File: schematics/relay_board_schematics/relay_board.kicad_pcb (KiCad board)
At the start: 2 copper layers, 45 x 75 mm, 46 parts, among them J1 Programming Header, Q1 MMBF170, Q2 MMBF170, U1 SPST_POWER_RELAY, U2 PIC16F1826-ISO, U3 dpdt_relay, U4 INA180A1, U5 CONN_01x05, U6 INA180A1, U7 CONN_01x05

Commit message: first attempt at rerouting
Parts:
- added D4: D, Diode_SMD:D_SMB_Handsoldering, B.Cu at (153.2, 78.2)
- added D5: BLUE 3.2V 10mA, LED_SMD:LED_1206_3216Metric_Pad1.42x1.75mm_HandSolder, F.Cu at (133.2, 133.5)
- added D6: D, Diode_SMD:D_SMB_Handsoldering, B.Cu at (141.1, 81.9)
- added D7: D, Diode_SMD:D_SMB_Handsoldering, B.Cu at (151.9, 83.0)
- C1, C2, C3: footprint Capacitor_SMD:C_0805_2012Metric_Pad1.15x1.40mm_HandSolder -> Capacitor_SMD:C_0805_2012Metric_Pad1.18x1.45mm_HandSolder
- D2: footprint Diode_THT:D_DO-35_SOD27_P7.62mm_Horizontal -> Diode_SMD:D_SMB_Handsoldering
- D3: footprint LED_SMD:LED_1206_3216Metric_Pad1.42x1.75mm_HandSolder -> Diode_SMD:D_SMB_Handsoldering; moved to B.Cu
- F1: footprint rlcs:littlefuse_01000020Z -> custom:littlefuse_01000020Z
- J1: footprint rlcs:PinHeader_5x2.54_SMD_90deg_952-3198-1-ND -> custom:PinHeader_5x2.54_SMD_90deg_952-3198-1-ND
- P1: renamed from GND      PWR
- P2: renamed from PWR      GND
- R1, R10, R11, R12, R13, R2, R3, R4, R5, R6, R7, R8, R9: footprint Resistor_SMD:R_0805_2012Metric_Pad1.15x1.40mm_HandSolder -> Resistor_SMD:R_0805_2012Metric_Pad1.20x1.40mm_HandSolder
- R14, R15: value 0.02 -> 0.01; footprint Resistor_SMD:R_2512_6332Metric_Pad1.52x3.35mm_HandSolder -> Resistor_SMD:R_2512_6332Metric_Pad1.40x3.35mm_HandSolder
- R16: value R -> 180; footprint Resistor_SMD:R_0805_2012Metric_Pad1.15x1.40mm_HandSolder -> Resistor_SMD:R_0805_2012Metric_Pad1.20x1.40mm_HandSolder
- SW1: renamed from 0   SW1   1; footprint rlcs:DIP_SWITCH_4X2 -> custom:DIP_SWITCH_4X2
- TP0: renamed from GND; footprint Socket_Strips:Socket_Strip_Straight_1x01_Pitch2.54mm -> custom:Socket_Strip_Straight_1x01_Pitch2.54mm
- TP1: renamed from 12V; footprint Socket_Strips:Socket_Strip_Straight_1x01_Pitch2.54mm -> custom:Socket_Strip_Straight_1x01_Pitch2.54mm
- TP2: renamed from 5V; footprint Socket_Strips:Socket_Strip_Straight_1x01_Pitch2.54mm -> custom:Socket_Strip_Straight_1x01_Pitch2.54mm
- TP3: renamed from POWER; footprint Socket_Strips:Socket_Strip_Straight_1x01_Pitch2.54mm -> custom:Socket_Strip_Straight_1x01_Pitch2.54mm
- U1: footprint rlcs:Relay_SPST_G5LE-1A -> custom:Relay_SPST_G5LE-1A
- U2: footprint rlcs:PIC16F1826-ISO -> custom:PIC16F1826-ISO
- U3: footprint rlcs:Relay_DPDT_RT424012F -> custom:Relay_DPDT_RT424012F
- moved D3 57.2 mm to (141.9, 77.1)
- moved C3 20.7 mm to (134.7, 97.5)
- moved C1 12.5 mm to (132.9, 111.4), turned to -90 degrees
- moved C2 8.75 mm to (137.4, 97.5), turned to 90 degrees
- moved P2 5.40 mm to (135.2, 128.9), turned to 90 degrees
- moved G*** 4.76 mm to (147.9, 133.2)
- moved R9 4.11 mm to (165.3, 77.2), turned to 180 degrees
- moved R5 3.70 mm to (163.7, 86.8)
- moved D2 3.54 mm to (148.5, 122.2)
- moved R8 3.16 mm to (159.5, 81.1)
- moved R7 2.46 mm to (159.9, 77.2), turned to 0 degrees
- moved TP2 2.31 mm to (132.1, 92.6)
- moved R13 2.27 mm to (159.6, 113.2), turned to 180 degrees
- moved R12 1.86 mm to (136.4, 132.8), turned to 90 degrees
- moved U4 1.84 mm to (134.1, 86.8)
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- renumbered ACT_PWR to P3
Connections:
- D3 pad 1: Net-(D3-Pad1) -> /G1
- D3 pad 2: Net-(D3-Pad2) -> GND
- P2 pad 1: GND -> Net-(F1-Pad1)
- P2 pad 2: Net-(F1-Pad1) -> GND
- R16 pad 1: Net-(D3-Pad1) -> Net-(D5-Pad1)
- U2 pad 11: Net-(D3-Pad2) -> Net-(D5-Pad2)
- U5 pad 1: /SDA -> +12V
- U5 pad 2: /SCL -> +5V
- U5 pad 4: +5V -> /SCL
- U5 pad 5: +12V -> /SDA
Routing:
- net +5V: track 227.5 -> 194.1 mm, vias 5 -> 3
- net Net-(D3-Pad2): track 29.4 -> 0.00 mm, vias 1 -> 0
- net Net-(D5-Pad2): track 0.00 -> 27.6 mm, vias 0 -> 3
- net GND: track 200.4 -> 186.5 mm, vias 8 -> 7
- net Net-(D5-Pad1): track 0.00 -> 8.02 mm
- net Net-(D3-Pad1): track 7.92 -> 0.00 mm
- net Net-(R14-Pad2): track 37.6 -> 29.8 mm
- net Net-(D2-Pad2): track 16.1 -> 23.6 mm
- net /G1: track 31.6 -> 39.0 mm
- net +12V: track 117.7 -> 110.6 mm
- net /G2: track 20.4 -> 26.5 mm
- net /P2: track 19.8 -> 24.5 mm
- net /CURR_SENSE_2: track 23.7 -> 27.9 mm
- net /SELECT: track 43.2 -> 39.1 mm
- net Net-(F1-Pad2): track 29.8 -> 26.4 mm
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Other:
- board text added: "RLCS Relay Board"
- board text removed: "P1"
- board text removed: "RLCS rev3 Hokkaido Aidan Ha 2020-02-02"

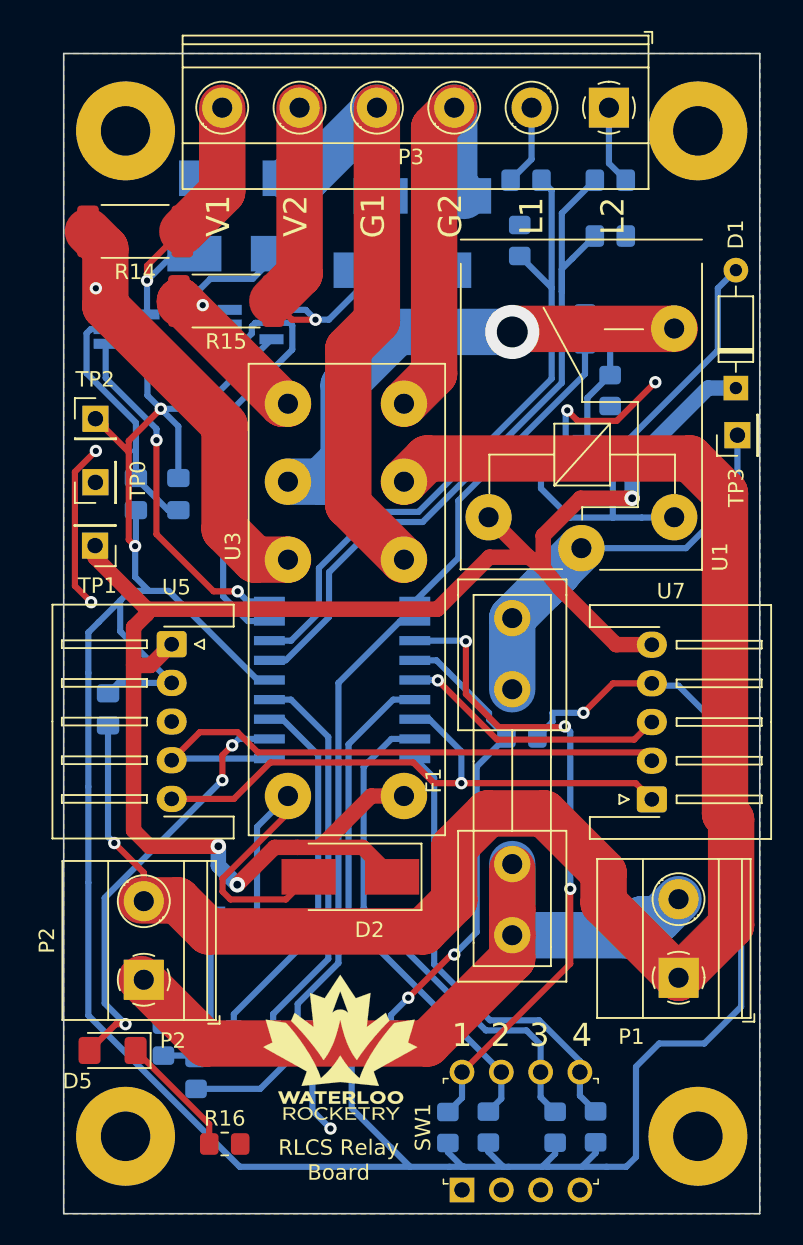
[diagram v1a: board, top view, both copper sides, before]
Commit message: fixed reversed 12V power connectors and cleaned up silkscreens
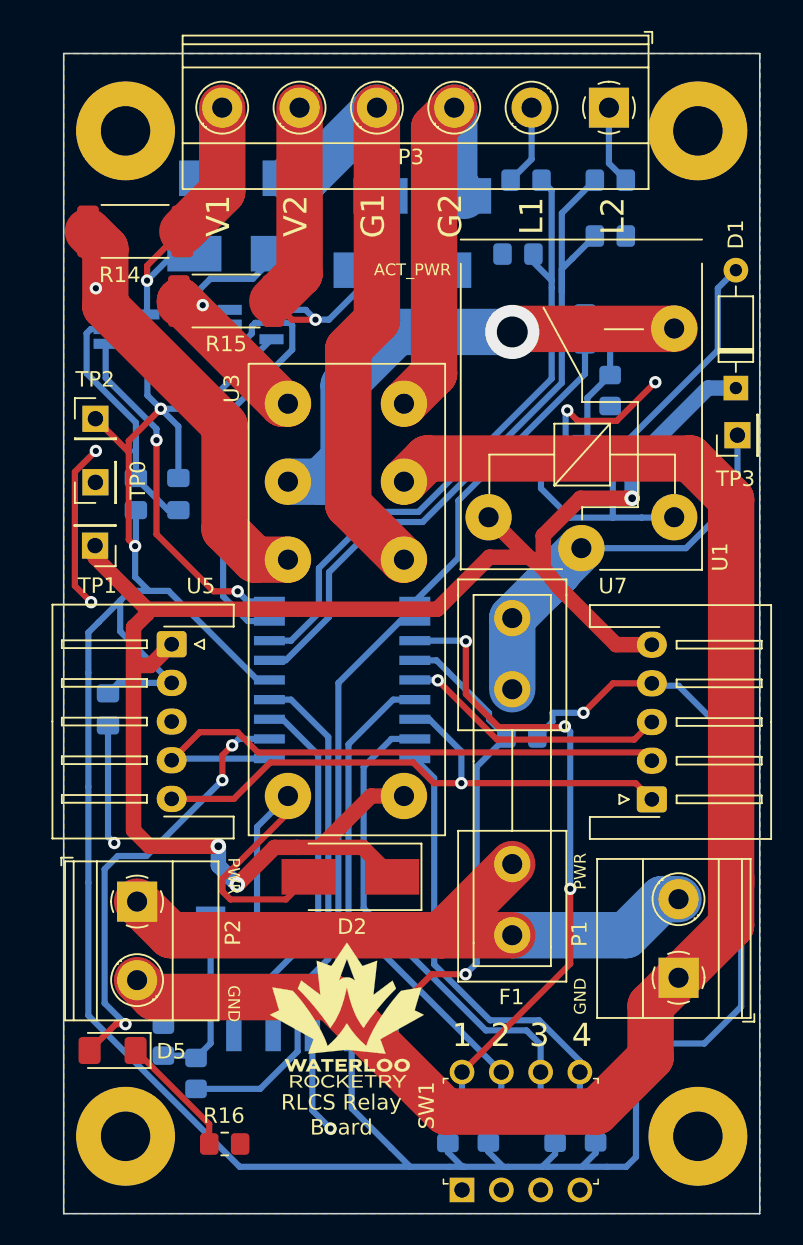
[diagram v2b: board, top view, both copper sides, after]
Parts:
- moved P2 5.07 mm to (134.7, 123.8), turned to -90 degrees
- moved G*** 2.13 mm to (148.3, 131.2)
- moved R8 0.89 mm to (159.4, 82.0), turned to 180 degrees
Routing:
- net Net-(F1-Pad1): track 50.1 -> 43.4 mm
- net GND: track 186.5 -> 180.3 mm
- net /~{MCLR}: track 30.7 -> 31.9 mm
- net Net-(D5-Pad2): track 27.6 -> 28.7 mm
- net +5V: track 194.1 -> 193.4 mm
- net /LIM1: track 43.0 -> 42.3 mm
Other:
- board text added: "ACT_PWR"
- board text added: "GND"
- board text added: "PWR"
- board text removed: "P2"

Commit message: addressed Jack's comments on pcb
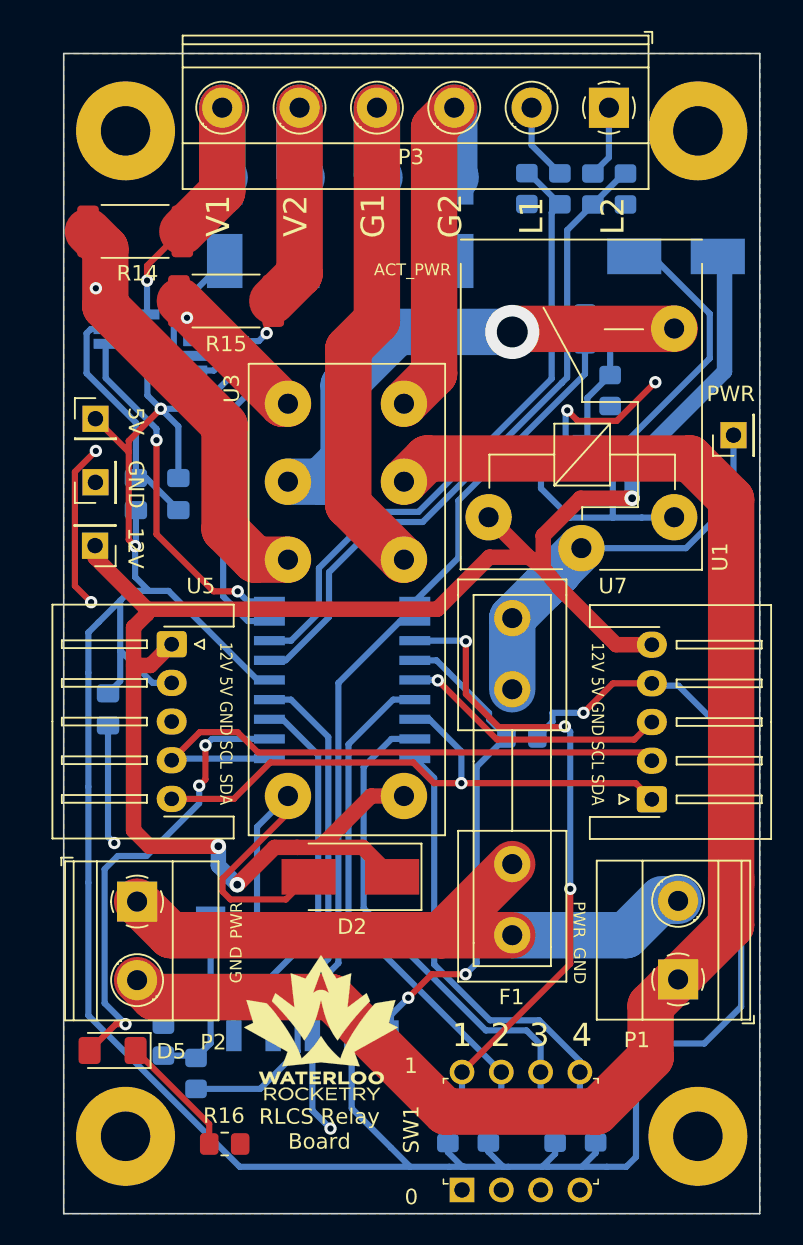
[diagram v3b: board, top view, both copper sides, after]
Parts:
- D1: footprint Diode_THT:D_DO-35_SOD27_P7.62mm_Horizontal -> Diode_SMD:D_SMB_Handsoldering; moved to B.Cu
- moved D1 9.35 mm to (169.6, 82.1), turned to 180 degrees
- moved D3 8.91 mm to (150.4, 79.7), turned to -90 degrees
- moved D7 7.30 mm to (145.4, 79.7), turned to -90 degrees
- moved R8 4.27 mm to (159.9, 77.7), turned to -90 degrees
- moved R10 3.19 mm to (166.3, 77.8), turned to -90 degrees
- moved U6 3.01 mm to (139.9, 88.5)
- moved D4 2.63 mm to (155.3, 79.7), turned to -90 degrees
- moved D6 2.35 mm to (140.4, 79.7), turned to -90 degrees
- moved R7 2.25 mm to (162.1, 77.7), turned to -90 degrees
- moved G*** 1.86 mm to (146.6, 132.0)
- moved R9 1.26 mm to (164.2, 77.8), turned to -90 degrees
- moved TP3 0.25 mm to (173.3, 93.7)
- moved P1 0.11 mm to (169.7, 128.9)
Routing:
- net +12V: track 110.5 -> 117.8 mm
- net +5V: track 193.4 -> 189.7 mm
- net /CURR_SENSE_2: track 27.8 -> 24.6 mm
- net /LIM2: track 46.5 -> 43.3 mm
- net /G1: track 39.0 -> 36.1 mm
- net Net-(D1-Pad2): track 30.8 -> 33.7 mm
- net /P2: track 24.5 -> 22.2 mm
- net GND: track 180.3 -> 178.3 mm
- net Net-(R15-Pad2): track 13.2 -> 11.5 mm
- net /G2: track 26.5 -> 25.0 mm
- net Net-(D5-Pad2): track 28.7 -> 29.7 mm
- net Net-(F1-Pad1): track 43.4 -> 44.4 mm
- net /LIM1: track 42.3 -> 41.4 mm
- net /P1: track 19.1 -> 19.9 mm
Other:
- board text added: "0"
- board text added: "12V"
- board text added: "5V"

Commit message: Reversed the 5-pin and 2-pin screw terminals to match CAN support board
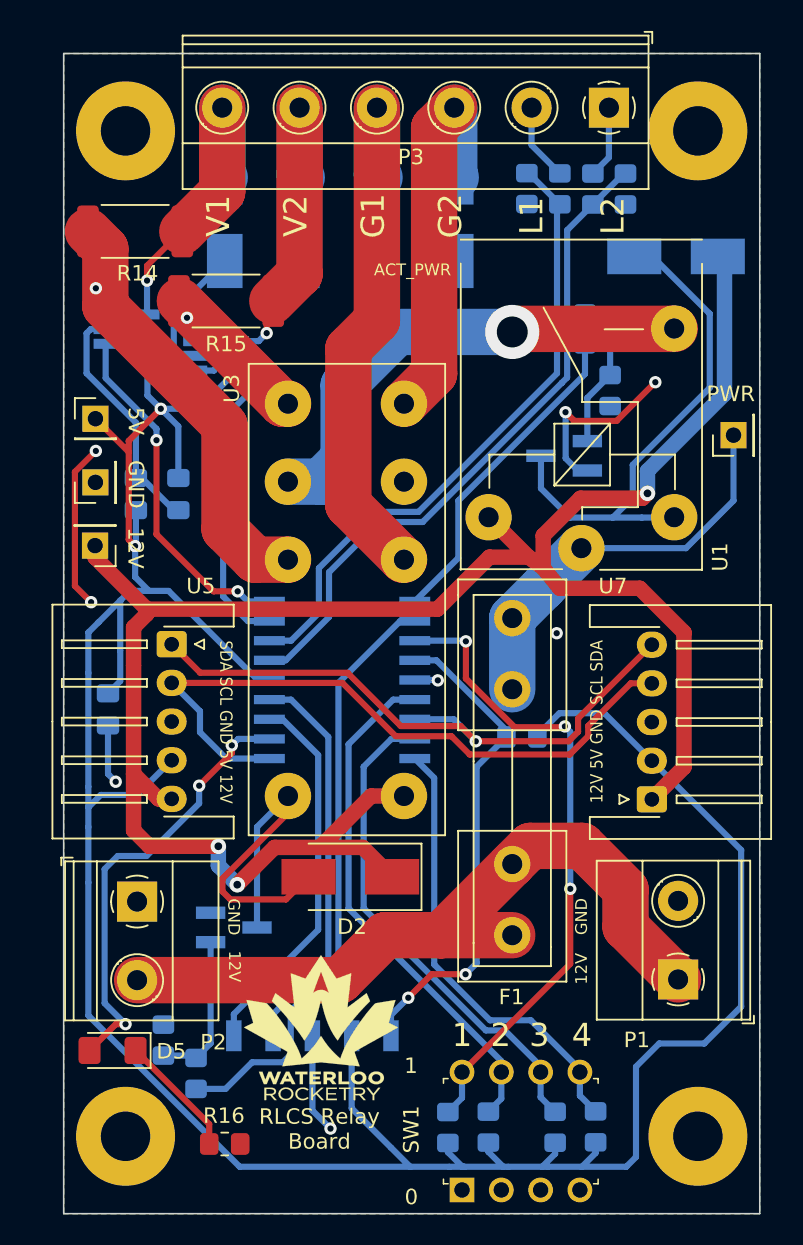
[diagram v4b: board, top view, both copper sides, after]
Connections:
- P1 pad 1: GND -> Net-(F1-Pad1)
- P1 pad 2: Net-(F1-Pad1) -> GND
- P2 pad 1: Net-(F1-Pad1) -> GND
- P2 pad 2: GND -> Net-(F1-Pad1)
- U5 pad 1: +12V -> /SDA
- U5 pad 2: +5V -> /SCL
- U5 pad 4: /SCL -> +5V
- U5 pad 5: /SDA -> +12V
- U7 pad 1: /SDA -> +12V
- U7 pad 2: /SCL -> +5V
- U7 pad 4: +5V -> /SCL
- U7 pad 5: +12V -> /SDA
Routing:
- net GND: track 178.3 -> 58.8 mm, vias 7 -> 8
- net +12V: track 117.8 -> 131.7 mm
- net /SCL: track 39.0 -> 44.4 mm
- net Net-(F1-Pad1): track 44.4 -> 48.2 mm
- net +5V: track 189.7 -> 186.8 mm, vias 3 -> 2
- net /SDA: track 38.9 -> 40.3 mm
- net Net-(D5-Pad2): track 29.7 -> 28.7 mm
- net /DIP_3: track 33.0 -> 32.2 mm
- net /DIP_1: track 42.4 -> 41.8 mm
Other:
- board text added: "SDA SCL GND 5V 12V"

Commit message: added missing decoupling cap to PIC VDD, moved decoupling caps closer to ICs, fixed main power connections, small tweaks to trace routing
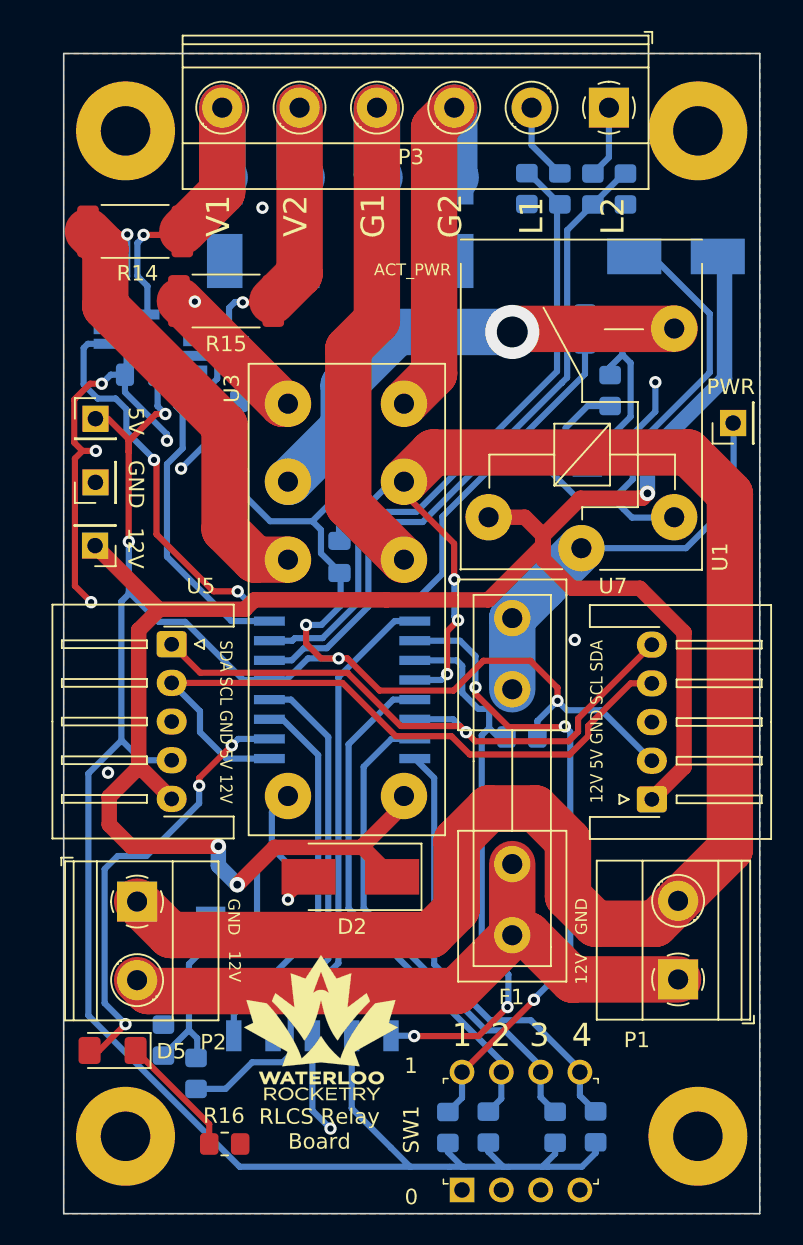
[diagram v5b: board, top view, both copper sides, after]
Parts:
- added C4: 0.1uF, Capacitor_SMD:C_0805_2012Metric_Pad1.18x1.45mm_HandSolder, B.Cu at (149.0, 97.5)
- moved C1 17.9 mm to (147.8, 101.5), turned to 90 degrees
- moved C3 7.72 mm to (135.0, 89.8), turned to 0 degrees
- moved C2 6.67 mm to (140.3, 91.5), turned to 0 degrees
- moved TP3 0.79 mm to (173.3, 92.9)
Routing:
- net GND: track 58.8 -> 181.5 mm, vias 8 -> 13
- net Net-(D2-Pad2): track 23.6 -> 15.1 mm, vias 0 -> 1
- net Net-(R14-Pad2): track 29.8 -> 38.0 mm
- net Net-(F1-Pad1): track 48.2 -> 42.6 mm
- net /~{MCLR}: track 31.9 -> 37.0 mm
- net +5V: track 186.8 -> 182.5 mm, vias 2 -> 5
- net Net-(Q1-Pad1): track 9.54 -> 13.4 mm
- net /CURR_SENSE_2: track 24.6 -> 21.8 mm
- net /CURR_SENSE_1: track 22.8 -> 25.3 mm
- net Net-(D1-Pad2): track 33.7 -> 31.5 mm
- net Net-(R15-Pad2): track 11.5 -> 13.3 mm
- net Net-(U1-Pad4): track 31.9 -> 30.7 mm
- net /P2: track 22.2 -> 23.4 mm
- net /P1: track 19.9 -> 20.9 mm
- net /SDA: track 40.3 -> 39.5 mm
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
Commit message: more trace routing edits
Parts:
- moved C4 16.7 mm to (139.6, 111.3)
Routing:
- net +12V: track 131.7 -> 120.1 mm, vias 3 -> 1
- net +5V: track 182.5 -> 172.8 mm
- net GND: track 181.5 -> 175.7 mm, vias 13 -> 11
- net /LIM2: track 44.0 -> 45.5 mm
- net /LIM1: track 42.0 -> 42.6 mm
